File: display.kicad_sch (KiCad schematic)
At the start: 4 parts, among them U1 MAX7221xWG, U3 CC56-12GWA, U4 CC56-12GWA

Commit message: Component hookup
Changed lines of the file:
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@@
 		)
 	)
-	(hierarchical_label "Display"
+	(hierarchical_label "SPI"
 		(shape input)
 		(at 68.58 105.41 180)

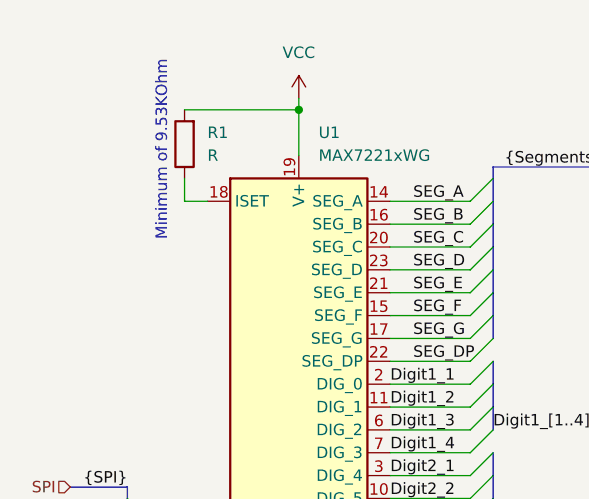
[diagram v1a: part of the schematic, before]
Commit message: Decoupling caps for ICs
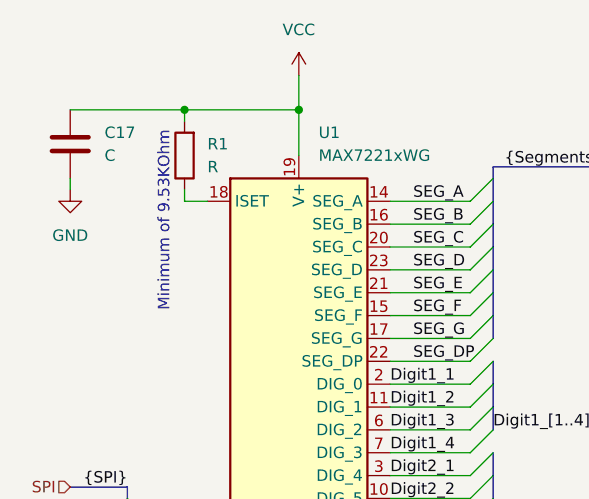
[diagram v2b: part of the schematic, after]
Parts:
- added C17: C, symbol Device:C
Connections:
- net GND: now also C17.2
- net VCC: now also C17.1
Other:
- moved on the sheet: R1
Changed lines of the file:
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@@
+		(color 0 0 0 0)
+	)
+	(junction
+		(at 81.28 63.5)
+		(diameter 0)
 		(color 0 0 0 0)
 	)
@@
 		)
 	)
+	(wire
+		(pts
+			(xy 81.28 63.5) (xy 68.58 63.5)
+		)
+		(stroke
+			(width 0)
+			(type default)
+		)
+	)
 	(bus
 		(pts
@@
 		)
 	)
-	(wire
-		(pts
-			(xy 93.98 62.23) (xy 93.98 63.5)
-		)
-		(stroke
-			(width 0)
-			(type default)
-		)
-	)
 	(bus
 		(pts
@@
 	(wire
 		(pts
+			(xy 81.28 64.77) (xy 81.28 63.5)
+		)
+		(stroke
+			(width 0)
+			(type default)
+		)
+	)
+	(wire
+		(pts
 			(xy 133.35 109.22) (xy 140.97 109.22)
 		)
@@
 	(wire
 		(pts
-			(xy 81.28 63.5) (xy 93.98 63.5)
-		)
-		(stroke
-			(width 0)
-			(type default)
-		)
-	)
-	(wire
-		(pts
 			(xy 196.85 121.92) (xy 205.74 121.92)
 		)
@@
 	(wire
 		(pts
+			(xy 93.98 59.69) (xy 93.98 63.5)
+		)
+		(stroke
+			(width 0)
+			(type default)
+		)
+	)
+	(wire
+		(pts
 			(xy 77.47 114.3) (xy 83.82 114.3)
 		)
@@
 		)
 	)
+	(wire
+		(pts
+			(xy 93.98 63.5) (xy 81.28 63.5)
+		)
+		(stroke
+			(width 0)
+			(type default)
+		)
+	)
+	(wire
+		(pts
+			(xy 68.58 71.12) (xy 68.58 72.39)
+		)
+		(stroke
+			(width 0)
+			(type default)
+		)
+	)
 	(bus
 		(pts
@@
 	(wire
 		(pts
-			(xy 81.28 71.12) (xy 81.28 73.66)
+			(xy 81.28 72.39) (xy 81.28 73.66)
 		)
 		(stroke
@@
 	(text "Minimum of 9.53KOhm"
 		(exclude_from_sim no)
-		(at 78.74 68.072 90)
+		(at 78.994 75.946 90)
 		(effects
 			(font
@@
 	(symbol
 		(lib_id "Device:R")
-		(at 81.28 67.31 180)
+		(at 81.28 68.58 180)
 		(unit 1)
 		(exclude_from_sim no)
@@
 		(fields_autoplaced yes)
 		(property "Reference" "R1"
-			(at 83.82 66.0399 0)
+			(at 83.82 67.3099 0)
 			(effects
 				(font
@@
 		)
 		(property "Value" "R"
-			(at 83.82 68.5799 0)
+			(at 83.82 69.8499 0)
 			(effects
 				(font
@@
 		)
 		(property "Footprint" ""
-			(at 83.058 67.31 90)
+			(at 83.058 68.58 90)
 			(effects
 				(font
@@
 		)
 		(property "Datasheet" "~"
-			(at 81.28 67.31 0)
+			(at 81.28 68.58 0)
 			(effects
 				(font
@@
 		)
 		(property "Description" "Resistor"
-			(at 81.28 67.31 0)
+			(at 81.28 68.58 0)
 			(effects
 				(font
@@
 				(path "/16b3e55a-9d75-49bf-a6fe-25414eb3d7da/672d503e-18e4-4d43-9df6-e02286c9b23c"
 					(reference "R1")
+					(unit 1)
+				)
+			)
+		)
+	)
+	(symbol
+		(lib_id "Device:C")
+		(at 68.58 67.31 0)
+		(unit 1)
+		(exclude_from_sim no)
+		(in_bom yes)
+		(on_board yes)
+		(dnp no)
+		(fields_autoplaced yes)
+		(property "Reference" "C17"
+			(at 72.39 66.0399 0)
+			(effects
+				(font
+					(size 1.27 1.27)
+				)
+				(justify left)
+			)
+		)
+		(property "Value" "C"
+			(at 72.39 68.5799 0)
+			(effects
+				(font
+					(size 1.27 1.27)
+				)
+				(justify left)
+			)
+		)
+		(property "Footprint" ""
+			(at 69.5452 71.12 0)
+			(effects
+				(font
+					(size 1.27 1.27)
+				)
+				(hide yes)
+			)
+		)
+		(property "Datasheet" "~"
+			(at 68.58 67.31 0)
+			(effects
+				(font
+					(size 1.27 1.27)
+				)
+				(hide yes)
+			)
+		)
+		(property "Description" "Unpolarized capacitor"
+			(at 68.58 67.31 0)
+			(effects
+				(font
+					(size 1.27 1.27)
+				)
+				(hide yes)
+			)
+		)
+		(pin "1"
+		)
+		(pin "2"
+		)
+		(instances
+			(project "LifeCounter"
+				(path "/16b3e55a-9d75-49bf-a6fe-25414eb3d7da/672d503e-18e4-4d43-9df6-e02286c9b23c"
+					(reference "C17")
 					(unit 1)
 				)
@@
 				(path "/16b3e55a-9d75-49bf-a6fe-25414eb3d7da/672d503e-18e4-4d43-9df6-e02286c9b23c"
 					(reference "U3")
+					(unit 1)
+				)
+			)
+		)
+	)
+	(symbol
+		(lib_id "power:GND")
+		(at 68.58 72.39 0)
+		(unit 1)
+		(exclude_from_sim no)
+		(in_bom yes)
+		(on_board yes)
+		(dnp no)
+		(fields_autoplaced yes)
+		(property "Reference" "#PWR046"
+			(at 68.58 78.74 0)
+			(effects
+				(font
+					(size 1.27 1.27)
+				)
+				(hide yes)
+			)
+		)
+		(property "Value" "GND"
+			(at 68.58 77.47 0)
+			(effects
+				(font
+					(size 1.27 1.27)
+				)
+			)
+		)
+		(property "Footprint" ""
+			(at 68.58 72.39 0)
+			(effects
+				(font
+					(size 1.27 1.27)
+				)
+				(hide yes)
+			)
+		)
+		(property "Datasheet" ""
+			(at 68.58 72.39 0)
+			(effects
+				(font
+					(size 1.27 1.27)
+				)
+				(hide yes)
+			)
+		)
+		(property "Description" "Power symbol creates a global label with name \"GND\" , ground"
+			(at 68.58 72.39 0)
+			(effects
+				(font
+					(size 1.27 1.27)
+				)
+				(hide yes)
+			)
+		)
+		(pin "1"
+		)
+		(instances
+			(project "LifeCounter"
+				(path "/16b3e55a-9d75-49bf-a6fe-25414eb3d7da/672d503e-18e4-4d43-9df6-e02286c9b23c"
+					(reference "#PWR046")
 					(unit 1)
 				)
@@
 	(symbol
 		(lib_id "power:VCC")
-		(at 93.98 62.23 0)
+		(at 93.98 59.69 0)
 		(unit 1)
 		(exclude_from_sim no)
@@
 		(fields_autoplaced yes)
 		(property "Reference" "#PWR01"
-			(at 93.98 66.04 0)
+			(at 93.98 63.5 0)
 			(effects
 				(font
@@
 		)
 		(property "Value" "VCC"
-			(at 93.98 57.15 0)
+			(at 93.98 54.61 0)
 			(effects
 				(font
@@
 		)
 		(property "Footprint" ""
-			(at 93.98 62.23 0)
+			(at 93.98 59.69 0)
 			(effects
 				(font
@@
 		)
 		(property "Datasheet" ""
-			(at 93.98 62.23 0)
+			(at 93.98 59.69 0)
 			(effects
 				(font
@@
 		)
 		(property "Description" "Power symbol creates a global label with name \"VCC\""
-			(at 93.98 62.23 0)
-			(effects
-				(font
+			(at 93.98 59.69 0)
+			(effects
+				(font

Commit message: Initial component placement
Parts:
- C17: footprint (none) -> Capacitor_SMD:C_0805_2012Metric_Pad1.18x1.45mm_HandSolder
- R1: footprint (none) -> Resistor_SMD:R_0805_2012Metric_Pad1.20x1.40mm_HandSolder
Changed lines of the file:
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@@
 			)
 		)
-		(property "Footprint" ""
+		(property "Footprint" "Resistor_SMD:R_0805_2012Metric_Pad1.20x1.40mm_HandSolder"
 			(at 83.058 68.58 90)
 			(effects
@@
 			)
 		)
-		(property "Footprint" ""
+		(property "Footprint" "Capacitor_SMD:C_0805_2012Metric_Pad1.18x1.45mm_HandSolder"
 			(at 69.5452 71.12 0)
 			(effects

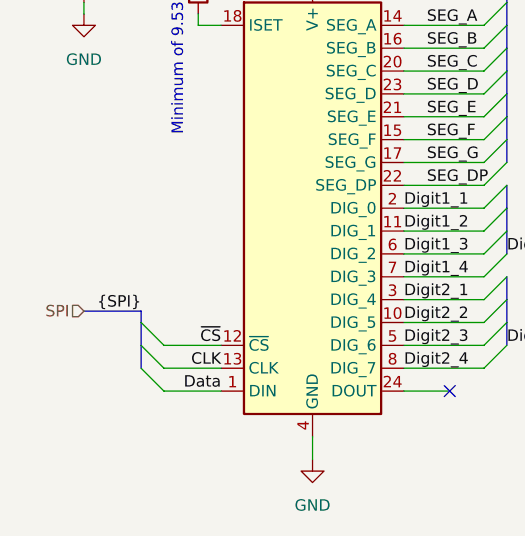
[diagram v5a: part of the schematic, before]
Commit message: Constant current sink to status LEDs and rewiring controller
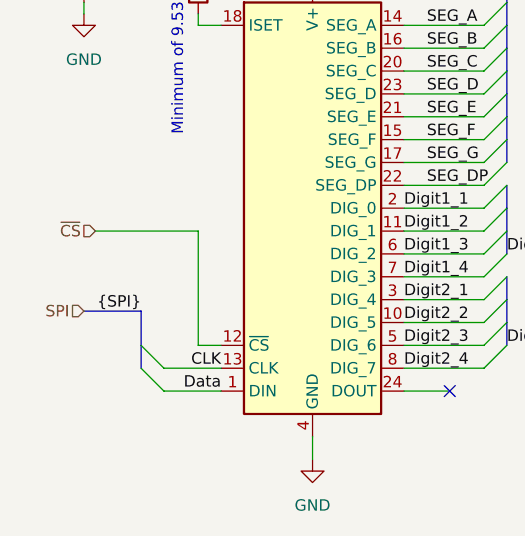
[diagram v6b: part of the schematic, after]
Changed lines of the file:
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@@
-	)
-	(bus_entry
-		(at 74.93 106.68)
-		(size 2.54 2.54)
-		(stroke
-			(width 0)
-			(type default)
-		)
 	)
 	(bus_entry
@@
 		)
 	)
-	(bus
-		(pts
-			(xy 74.93 105.41) (xy 74.93 106.68)
-		)
-		(stroke
-			(width 0)
-			(type default)
-		)
-	)
 	(wire
 		(pts
@@
 	(wire
 		(pts
+			(xy 69.85 96.52) (xy 81.28 96.52)
+		)
+		(stroke
+			(width 0)
+			(type default)
+		)
+	)
+	(wire
+		(pts
 			(xy 104.14 106.68) (xy 113.03 106.68)
 		)
@@
 		)
 	)
+	(wire
+		(pts
+			(xy 81.28 109.22) (xy 81.28 96.52)
+		)
+		(stroke
+			(width 0)
+			(type default)
+		)
+	)
 	(bus
 		(pts
@@
 	(bus
 		(pts
-			(xy 74.93 106.68) (xy 74.93 109.22)
+			(xy 74.93 105.41) (xy 74.93 109.22)
 		)
 		(stroke
@@
 	(wire
 		(pts
-			(xy 77.47 109.22) (xy 83.82 109.22)
-		)
-		(stroke
-			(width 0)
-			(type default)
-		)
-	)
-	(wire
-		(pts
 			(xy 104.14 88.9) (xy 113.03 88.9)
 		)
@@
 		(pts
 			(xy 104.14 96.52) (xy 113.03 96.52)
+		)
+		(stroke
+			(width 0)
+			(type default)
+		)
+	)
+	(wire
+		(pts
+			(xy 83.82 109.22) (xy 81.28 109.22)
 		)
 		(stroke
@@
 		)
 	)
-	(label "~{CS}"
-		(at 83.82 109.22 180)
-		(effects
-			(font
-				(size 1.27 1.27)
-			)
-			(justify right bottom)
-		)
-	)
 	(label "Digit2_3"
 		(at 104.14 109.22 0)
@@
 		)
 	)
+	(hierarchical_label "~{CS}"
+		(shape input)
+		(at 69.85 96.52 180)
+		(effects
+			(font
+				(size 1.27 1.27)
+			)
+			(justify right)
+		)
+	)

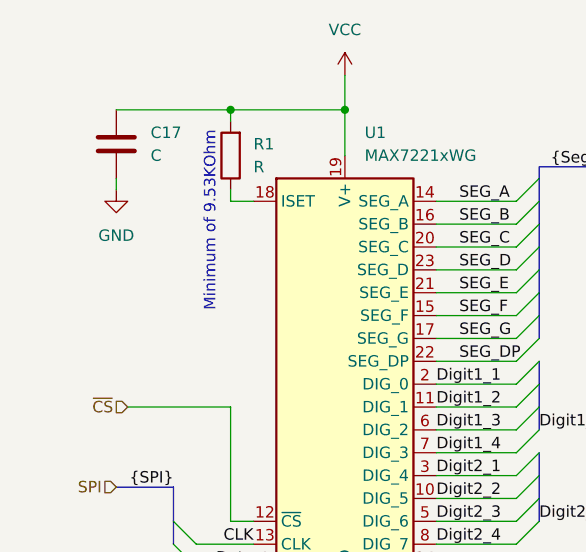
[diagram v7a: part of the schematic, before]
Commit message: Assign component values to display passives
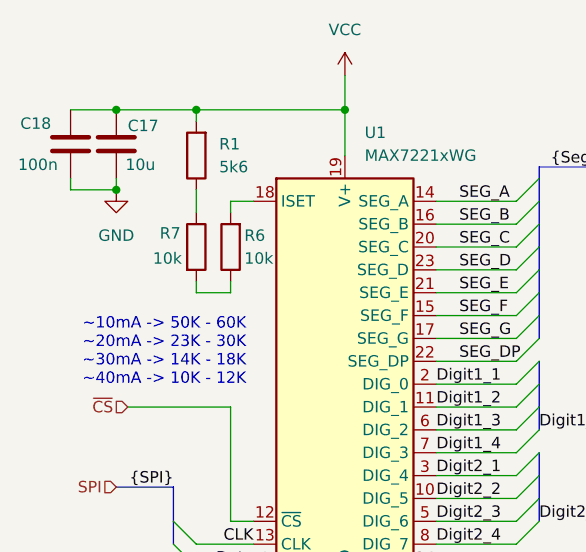
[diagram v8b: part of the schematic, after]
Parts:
- added C18: 100n, Capacitor_SMD:C_0805_2012Metric_Pad1.18x1.45mm_HandSolder, symbol Device:C
- added R6, R7: 10k, Resistor_SMD:R_0805_2012Metric_Pad1.20x1.40mm_HandSolder, symbol Device:R
- C17: value C -> 10u
- R1: value R -> 5k6
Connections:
- net GND: now also C18.2
- net VCC: now also C18.1
- net at R1.1: now also R7.1; no longer U1.18 (ISET)
- new net: R6.1, R7.2
- new net: R6.2, U1.18 (ISET)
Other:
- note added: "~10mA -> 50K - 60K ~20mA -> 23K - 30K ~30mA -> 14K - 18K ~40mA -> 10K - 12K"
- note removed: "Minimum of 9.53KOhm"
- moved on the sheet: R1
